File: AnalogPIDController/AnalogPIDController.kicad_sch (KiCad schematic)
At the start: 0 parts

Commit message: added op amp
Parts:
- added D1: LED, ECE319K:LED_D5.0mm, symbol ECE319K:LED
- added R1: R_US, symbol Device:R_US
- added R2, R3, R4, R5: 10k, symbol Device:R_US
- added U1: TL082, symbol Amplifier_Operational:TL082
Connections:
- new net: R3.1, U1.1
- new net: R2.2, R3.2, U1.2 (-)
- new net: R4.1, R5.1, U1.3 (+)
- new net: D1.2 (A), R1.2, R2.1
- new net +3.3V: R1.1
- new net GND: D1.1 (K), R5.2
- new net Vset: R4.2
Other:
- note added: "Proportional Integrator Differentiator"
- note added: "Vout = Vset - Vcurr = (e(t))"

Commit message: Finished Some of PID schematic
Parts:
- added C1, C2: C_Small, symbol Device:C_Small
- added R6, R7, R8, R9: R_US, symbol Device:R_US
- added RV1, RV3, RV4: R_Potentiometer_US, symbol Device:R_Potentiometer_US
- added U2: TL084, symbol Amplifier_Operational:TL084
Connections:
- net GND: now also RV1.1, RV3.1, RV4.1, U2.10 (+), U2.3 (+), U2.5 (+)
- net at R3.1, U1.1: now also C2.1, R6.1, RV3.3
- new net: C1.1, RV3.2, U2.6 (-)
- new net: C1.2, R8.1, U2.7
- new net: R9.1, RV4.2, U2.8
- new net: C2.2, RV4.3, U2.9 (-)
- new net: R7.1, RV1.2, U2.1
- new net: R6.2, RV1.3, U2.2 (-)

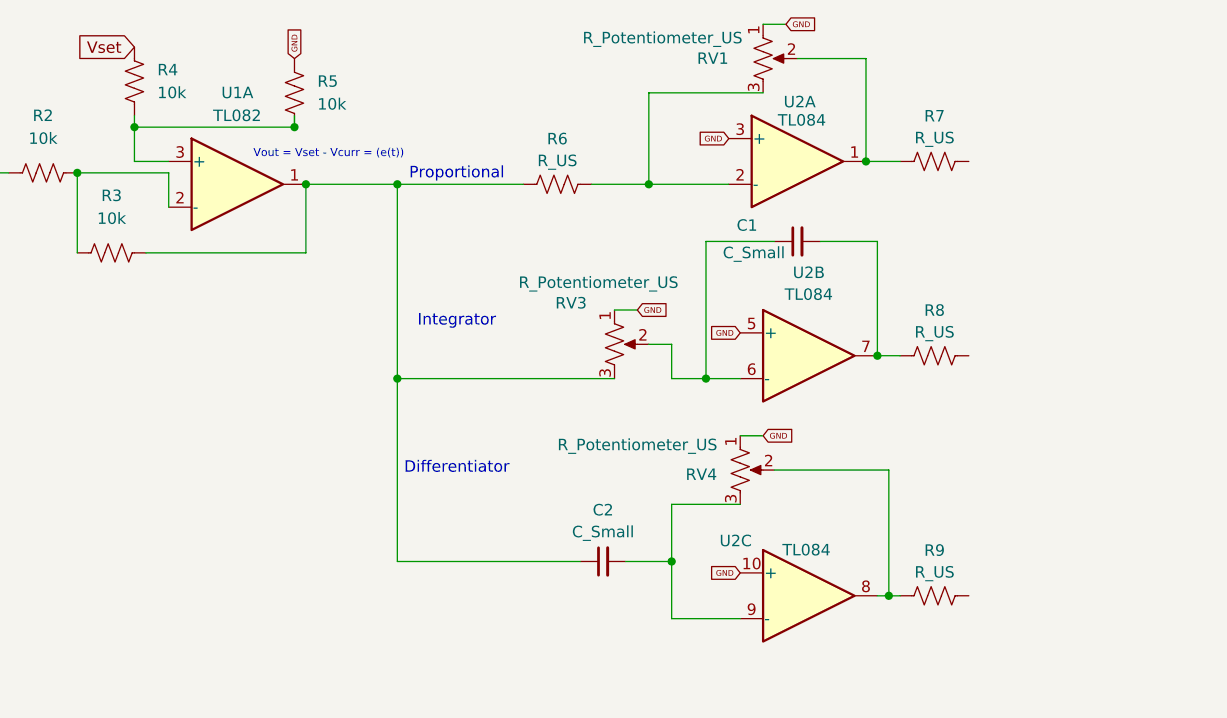
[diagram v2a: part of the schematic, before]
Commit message: added inv summer along with pid
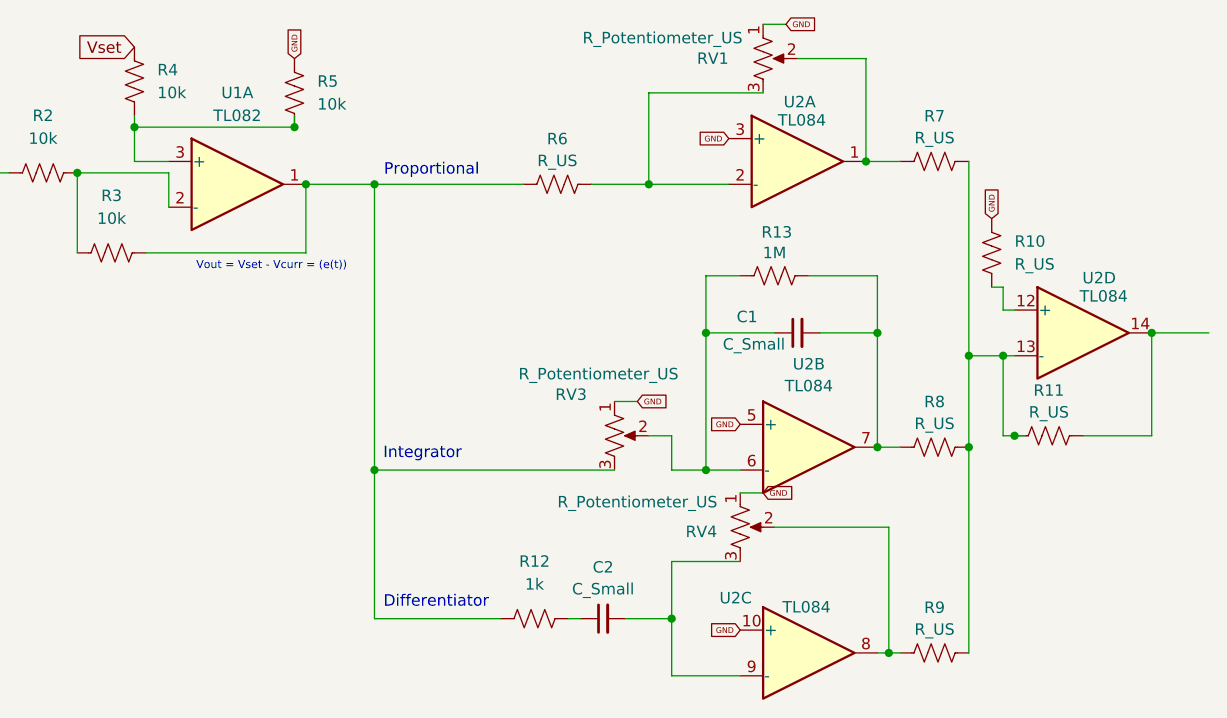
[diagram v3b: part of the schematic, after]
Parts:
- added R10, R11: R_US, symbol Device:R_US
- added R12: 1k, symbol Device:R_US
- added R13: 1M, symbol Device:R_US
- added unit 4 of U2
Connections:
- net GND: now also R10.2
- net at R3.1, R6.1, RV3.3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: now also R12.1; no longer C2.1
- net at C1.1, RV3.2, U2.6 (-): now also R13.1
- net at C1.2, R8.1, U2.7: now also R13.2
- net at R8.2: now also R7.2, R9.2, R11.1, U2.13 (-)
- new net: R11.2, U2.14
- new net: R10.1, U2.12 (+)
- new net: C2.1, R12.2
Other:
- note added: "Differentiator"
- note added: "Integrator"
- note added: "Proportional"
- note removed: "Proportional Integrator Differentiator"
- moved on the sheet: C1, C2, R8, R9, RV3, RV4, U2B, U2C

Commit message: fixed our idea, added transistor driver section, added some Vcurr led diff. amp circuit, and ideal LED voltage Vset
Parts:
- removed D1: LED, ECE319K:LED_D5.0mm, symbol ECE319K:LED
- added D1, D2: LED, symbol Device:LED
- added Q1: Q_NPN, symbol Device:Q_NPN
- added R14: 1k, symbol Device:R_US
- added R15, R17, R18: 10k, symbol Device:R_US
- added R16, R19: R_US, symbol Device:R_US
- added unit 2 of U1
- added unit 3 of U1
- added unit 5 of U2
- R1: value R_US -> 10k
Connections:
- net GND: now also D1.1 (K), Q1.E, R15.2
- net Vset: now also D1.2 (A), R19.2
- net at R11.2, U2.14: now also R14.1
- net at R1.2: now also R17.2, U1.6 (-); no longer R2.1
- net +3.3V renamed Vcathode
- net Vcathode: now also D2.1 (K), Q1.C
- new net: R18.1, U1.5 (+)
- new net: Q1.B, R14.2, R15.1
- new net: D2.2 (A), R16.1
- new net 3.3v: R19.1
- new net Vanode: R18.2
- new net VccLED: R16.2
- new net Vcurr: R17.1, R2.1, U1.7
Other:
- note added: "Ideal LED Voltage Vset"
- note added: "Power Rails and Vcc"
- note added: "Voltage Across LED = Vcurr"

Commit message: stuff
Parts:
- removed R5: 10k, symbol Device:R_US
- added C3, C5: 1u, symbol Device:C_Small
- added C4, C6: 0.1u, symbol Device:C_Small
- C1: value C_Small -> 10u
- C2: value C_Small -> 1n
- R10, R11, R6, R7, R8, R9: value R_US -> 10k
- R12: value 1k -> 100k
- R14: value 1k -> 2.2k
- R16: value R_US -> 620
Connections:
- net 3.3v is gone; now on net VCC: R19.1
- net VccLED is gone; now on net VCC: R16.2
- net GND: now also U1.4 (V-), U2.11 (V-), C3.1, C4.1, C5.1, C6.1
- net VCC: now reaches U2.4 (V+)
- net VCC: now also U1.8 (V+)
- new net: C3.2, C4.2
- new net: C5.2, C6.2
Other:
- moved on the sheet: D2, Q1, R14, R15, R16, U1C, U2E

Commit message: fixes
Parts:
- added C7: 2.7n, symbol Device:C_Small
- C2: value 1n -> 220n
- R12: value 100k -> 10k
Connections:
- net at R9.1, RV4.2, U2.8: now also C7.2
- net at C2.2, RV4.3, U2.9 (-): now also C7.1
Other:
- moved on the sheet: C2, C5, C6, R12, R9, RV4, U2C, U2E

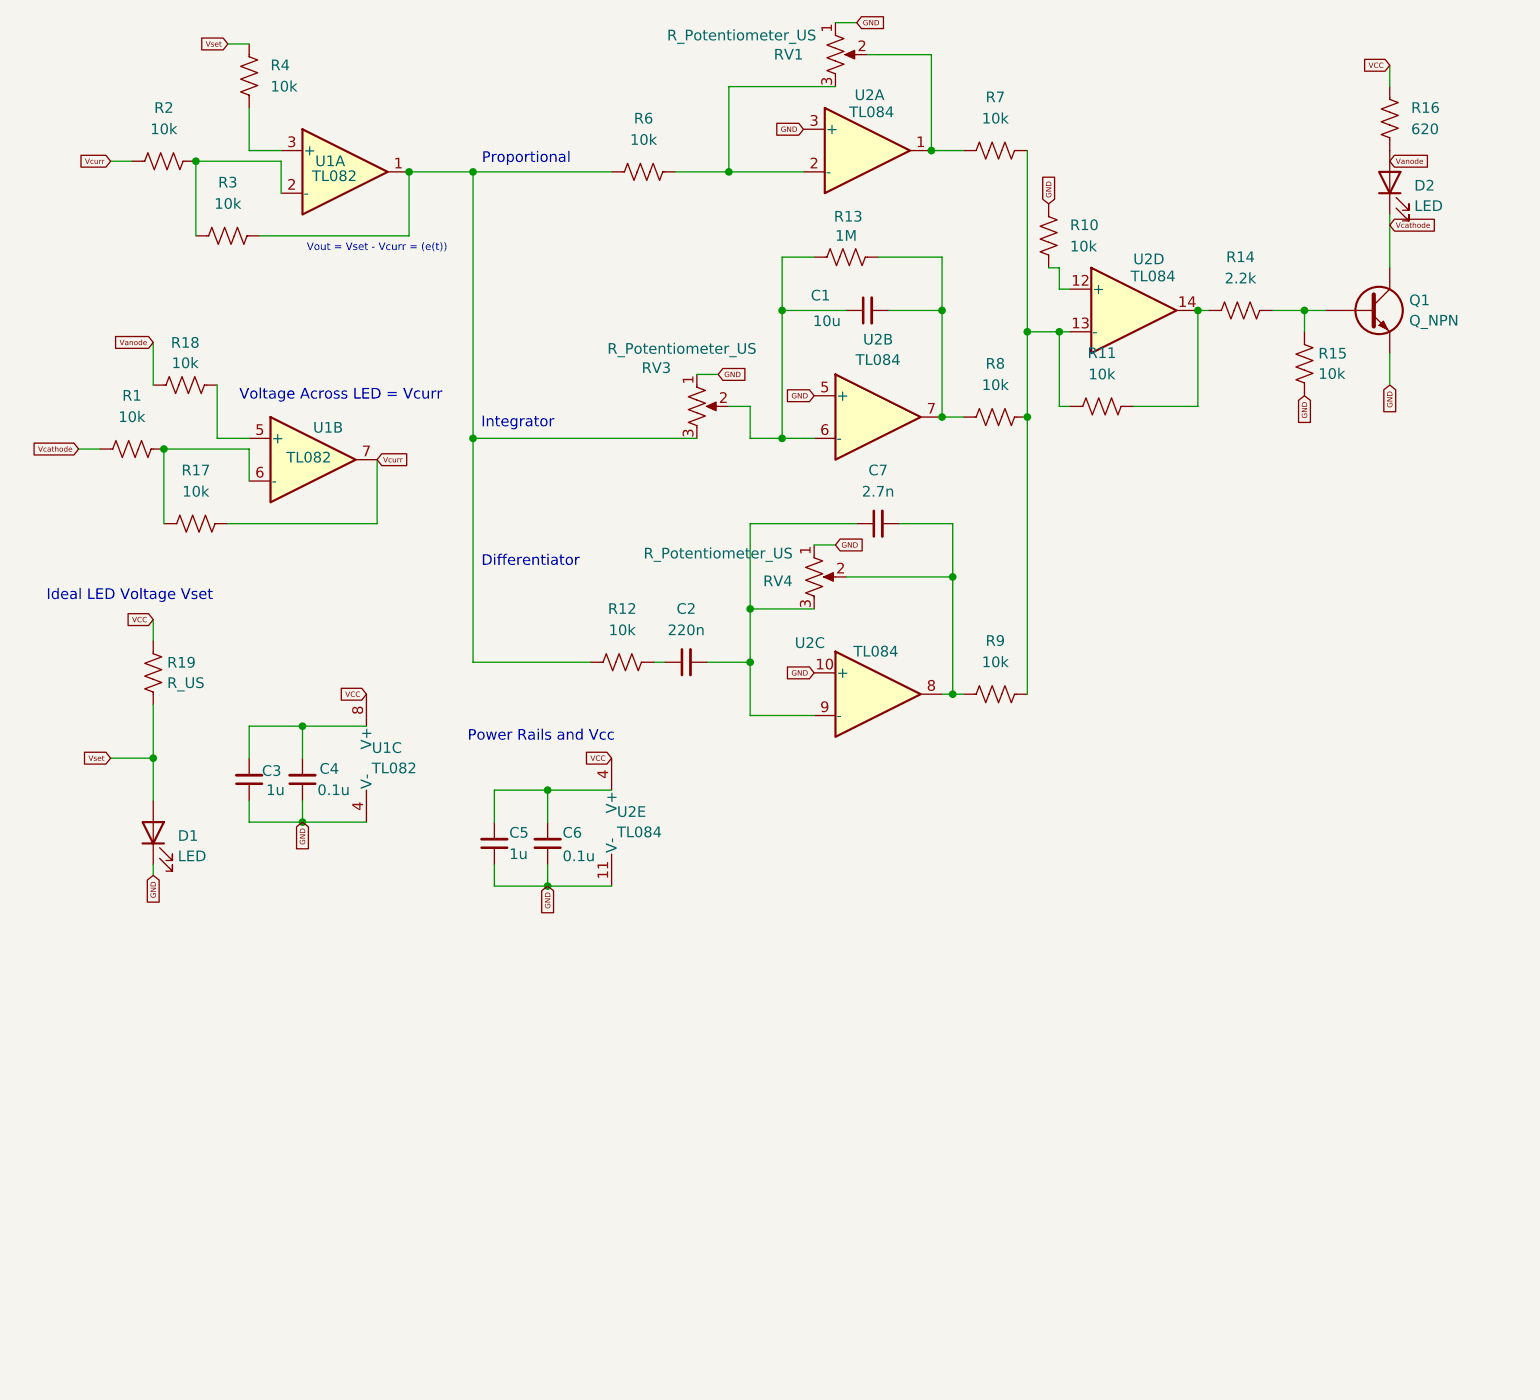
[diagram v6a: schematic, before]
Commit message: Added testpoints and no erc errors rn
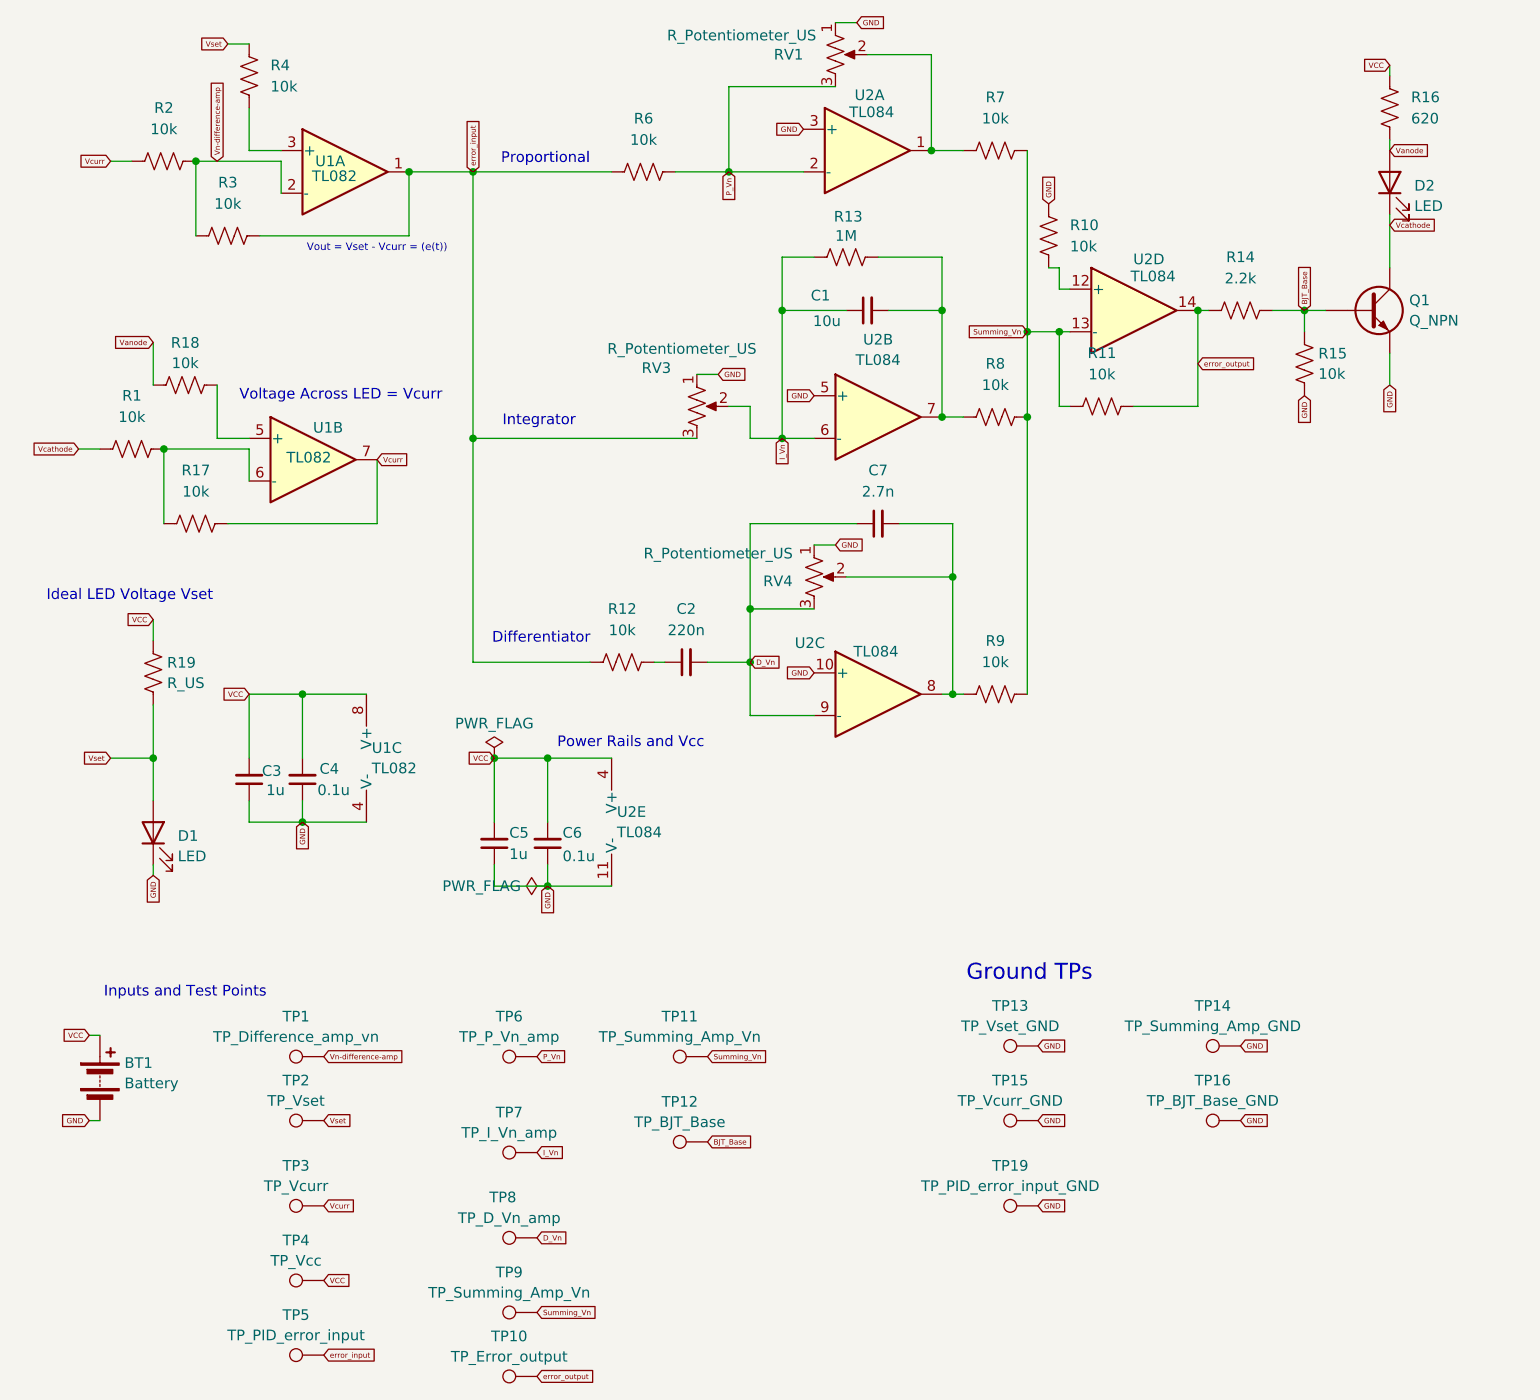
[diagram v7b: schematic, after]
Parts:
- added BT1: Battery, symbol Device:Battery
- added TP1: TP_Difference_amp_vn, symbol Connector:TestPoint
- added TP10: TP_Error_output, symbol Connector:TestPoint
- added TP11, TP9: TP_Summing_Amp_Vn, symbol Connector:TestPoint
- added TP12: TP_BJT_Base, symbol Connector:TestPoint
- added TP13: TP_Vset_GND, symbol Connector:TestPoint
- added TP14: TP_Summing_Amp_GND, symbol Connector:TestPoint
- added TP15: TP_Vcurr_GND, symbol Connector:TestPoint
- added TP16: TP_BJT_Base_GND, symbol Connector:TestPoint
- added TP19: TP_PID_error_input_GND, symbol Connector:TestPoint
- added TP2: TP_Vset, symbol Connector:TestPoint
- added TP3: TP_Vcurr, symbol Connector:TestPoint
- added TP4: TP_Vcc, symbol Connector:TestPoint
- added TP5: TP_PID_error_input, symbol Connector:TestPoint
- added TP6: TP_P_Vn_amp, symbol Connector:TestPoint
- added TP7: TP_I_Vn_amp, symbol Connector:TestPoint
- added TP8: TP_D_Vn_amp, symbol Connector:TestPoint
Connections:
- net GND: now also BT1.2 (-), TP13.1, TP14.1, TP15.1, TP16.1, TP19.1
- net VCC: now also C3.2, C4.2, C5.2, C6.2, BT1.1 (+), TP4.1
- net Vanode: now also D2.2 (A), R16.1
- net Vcurr: now also TP3.1
- net Vset: now also TP2.1
- net error_input: now reaches R12.1, R3.1, R6.1, RV3.3, U1.1
- net error_input: now also TP5.1
- net Vn-difference-amp: now reaches R2.2, R3.2, U1.2 (-)
- net Vn-difference-amp: now also TP1.1
- net I_Vn: now reaches C1.1, R13.1, RV3.2, U2.6 (-)
- net I_Vn: now also TP7.1
- net Summing_Vn: now reaches R11.1, R7.2, R8.2, R9.2, U2.13 (-)
- net Summing_Vn: now also TP11.1, TP9.1
- net error_output: now reaches R11.2, R14.1, U2.14
- net error_output: now also TP10.1
- net BJT_Base: now reaches Q1.B, R14.2, R15.1
- net BJT_Base: now also TP12.1
- net D_Vn: now reaches C2.2, C7.1, RV4.3, U2.9 (-)
- net D_Vn: now also TP8.1
- net P_Vn: now reaches R6.2, RV1.3, U2.2 (-)
- net P_Vn: now also TP6.1
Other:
- note added: "Ground TPs"
- note added: "Inputs and Test Points"
- moved on the sheet: R16

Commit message: Assigned some footprints
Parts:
- BT1: footprint (none) -> TerminalBlock_Phoenix:TerminalBlock_Phoenix_MKDS-1,5-2-5.08_1x02_P5.08mm_Horizontal
- C1: renamed from C3; footprint (none) -> Capacitor_THT:C_Disc_D3.8mm_W2.6mm_P2.50mm
- C2: renamed from C4; footprint (none) -> Capacitor_THT:C_Disc_D3.8mm_W2.6mm_P2.50mm
- C3: renamed from C5; footprint (none) -> Capacitor_THT:C_Disc_D3.8mm_W2.6mm_P2.50mm
- C4: renamed from C6; footprint (none) -> Capacitor_THT:C_Disc_D3.8mm_W2.6mm_P2.50mm
- C5: renamed from C2; footprint (none) -> Capacitor_THT:C_Disc_D3.8mm_W2.6mm_P2.50mm
- C6: renamed from C1; footprint (none) -> Capacitor_THT:C_Disc_D3.8mm_W2.6mm_P2.50mm
- C7: footprint (none) -> Capacitor_THT:C_Disc_D3.8mm_W2.6mm_P2.50mm
- D1, D2: footprint (none) -> LED_THT:LED_D1.8mm_W1.8mm_H2.4mm_Horizontal_O6.35mm_Z4.9mm
- Q1: footprint (none) -> 2N3904:TO92254P460H750-3
- R1: footprint (none) -> Resistor_THT:R_Axial_DIN0207_L6.3mm_D2.5mm_P10.16mm_Horizontal
- R10: renamed from R13; footprint (none) -> Resistor_THT:R_Axial_DIN0207_L6.3mm_D2.5mm_P10.16mm_Horizontal
- R11: renamed from R7; footprint (none) -> Resistor_THT:R_Axial_DIN0207_L6.3mm_D2.5mm_P10.16mm_Horizontal
- R12: renamed from R8; footprint (none) -> Resistor_THT:R_Axial_DIN0207_L6.3mm_D2.5mm_P10.16mm_Horizontal
- R13: renamed from R9; footprint (none) -> Resistor_THT:R_Axial_DIN0207_L6.3mm_D2.5mm_P10.16mm_Horizontal
- R14: renamed from R10; footprint (none) -> Resistor_THT:R_Axial_DIN0207_L6.3mm_D2.5mm_P10.16mm_Horizontal
- R15: renamed from R11; footprint (none) -> Resistor_THT:R_Axial_DIN0207_L6.3mm_D2.5mm_P10.16mm_Horizontal
- R16: renamed from R14; footprint (none) -> Resistor_THT:R_Axial_DIN0207_L6.3mm_D2.5mm_P10.16mm_Horizontal
- R17: renamed from R15; footprint (none) -> Resistor_THT:R_Axial_DIN0207_L6.3mm_D2.5mm_P10.16mm_Horizontal
- R18: renamed from R16; footprint (none) -> Resistor_THT:R_Axial_DIN0207_L6.3mm_D2.5mm_P10.16mm_Horizontal
- R2: renamed from R19; footprint (none) -> Resistor_THT:R_Axial_DIN0207_L6.3mm_D2.5mm_P10.16mm_Horizontal
- R3: renamed from R2; footprint (none) -> Resistor_THT:R_Axial_DIN0207_L6.3mm_D2.5mm_P10.16mm_Horizontal
- R4: renamed from R18; footprint (none) -> Resistor_THT:R_Axial_DIN0207_L6.3mm_D2.5mm_P10.16mm_Horizontal
- R5: renamed from R17; footprint (none) -> Resistor_THT:R_Axial_DIN0207_L6.3mm_D2.5mm_P10.16mm_Horizontal
- R6: renamed from R3; footprint (none) -> Resistor_THT:R_Axial_DIN0207_L6.3mm_D2.5mm_P10.16mm_Horizontal
- R7: renamed from R4; footprint (none) -> Resistor_THT:R_Axial_DIN0207_L6.3mm_D2.5mm_P10.16mm_Horizontal
- R8: renamed from R12; footprint (none) -> Resistor_THT:R_Axial_DIN0207_L6.3mm_D2.5mm_P10.16mm_Horizontal
- R9: renamed from R6; footprint (none) -> Resistor_THT:R_Axial_DIN0207_L6.3mm_D2.5mm_P10.16mm_Horizontal
- renumbered RV3 to RV1, RV4 to RV2, RV1 to RV3, TP15 to TP14, TP19 to TP15, TP14 to TP16, TP16 to TP17
